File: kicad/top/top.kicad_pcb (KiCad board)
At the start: 2 copper layers, 65 x 120 mm, 34 parts, among them J1 OLED_128x32, J2 Conn_01x15, SW1 SLW-864574-5A-RA-N-D, SW2 RotaryEncoder_Switch

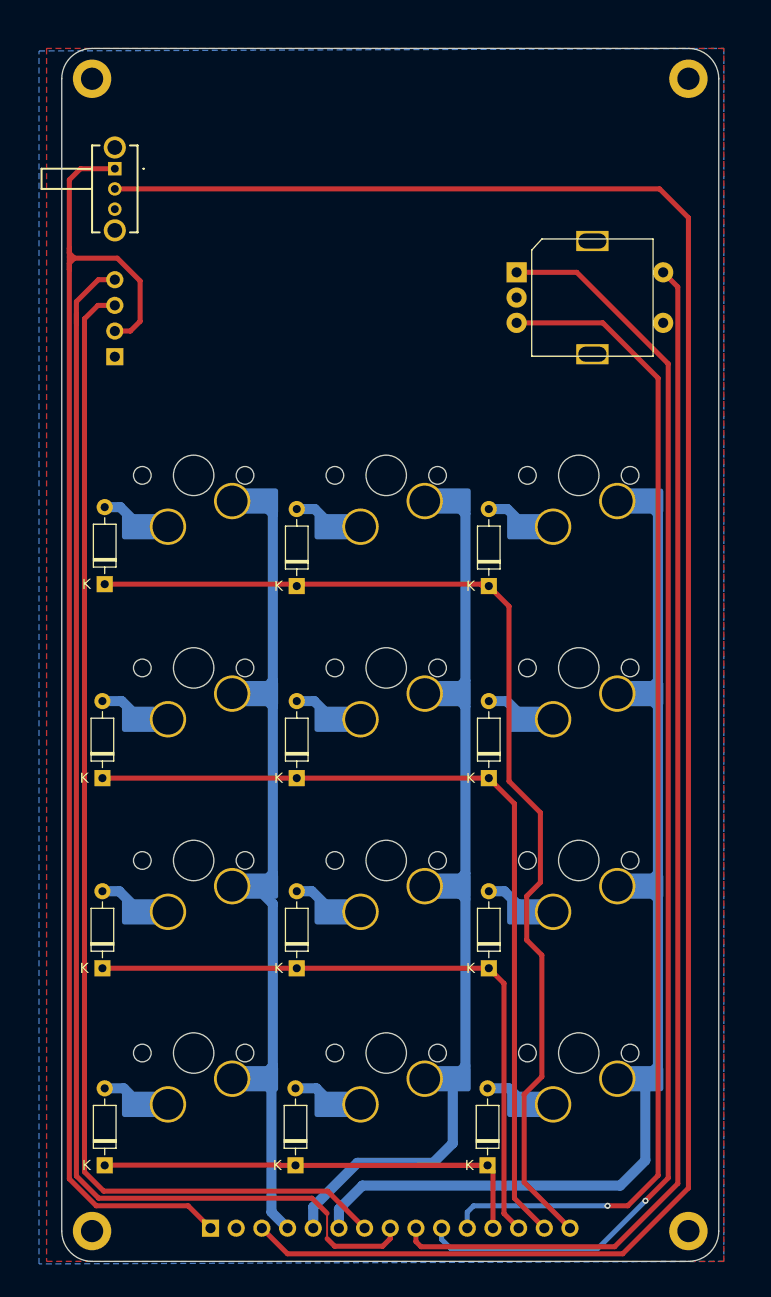
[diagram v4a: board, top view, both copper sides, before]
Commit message: Update KiCad project files and documentation
- Adjusted pad dimensions in top.kicad_pro:
  - Drill size changed from 1.0 to 0.8
  - Height changed from 1.7 to 1.6
  - Width changed from 1.7 to 2.0
- Modified design rule for isolated copper from "warning" to "ignore"
- Increased minimum hole clearance from 0.16 to 0.25

- Corrected global label positions for OLED_SDA and OLED_SCL in top.kicad_sch
- Updated footprint properties for mounting holes in top.kicad_sch to "MountingHole:MountingHole_2.5mm_Pad"

- Created new documentation file for component details.
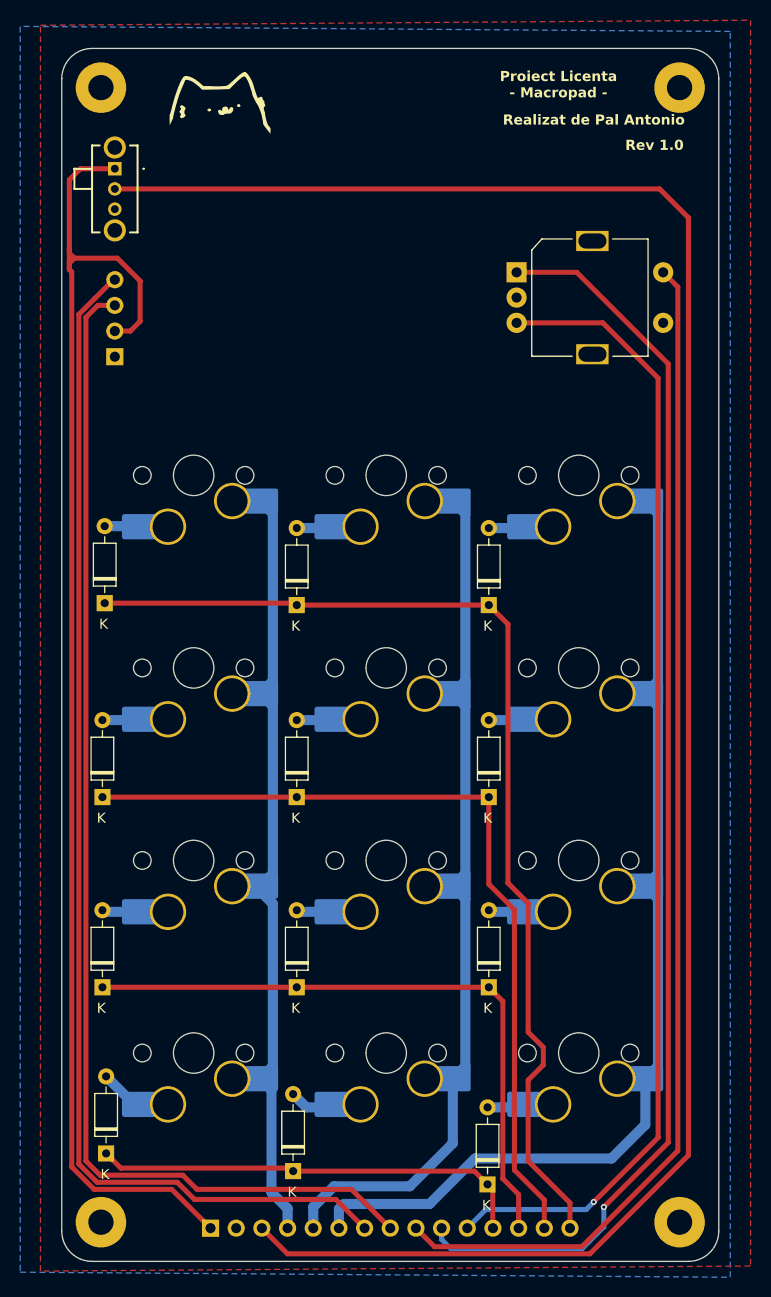
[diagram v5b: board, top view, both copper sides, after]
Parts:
- removed G***: LOGO, Project-Footprints:nubcat_10mm
- removed G***: LOGO, Project-Footprints:nubcat4_24mm
- added REF**: LOGO, Top-Footprints:nubcat_10mm, F.Cu at (133.3, 31.6)
- H1, H2, H3, H4: footprint Top-Footprints:MountingHole_2.2mm_M2_DIN965_Pad -> MountingHole:MountingHole_2.5mm_Pad
- moved D1 1.88 mm to (121.9, 80.9)
- moved D2 1.88 mm to (140.9, 81.1)
- moved D3 1.88 mm to (159.9, 81.1)
- moved D4 1.88 mm to (121.7, 100.1)
- moved D5 1.88 mm to (140.9, 100.1)
- moved D6 1.88 mm to (159.9, 100.1)
- moved D7 1.88 mm to (121.7, 118.9)
- moved D8 1.88 mm to (140.9, 118.9)
- moved D9 1.88 mm to (159.9, 118.9)
- moved D12 1.88 mm to (159.8, 138.4)
- moved H3 1.24 mm to (121.5, 142.2)
- moved H4 1.24 mm to (178.8, 142.2)
- moved H1 1.24 mm to (178.8, 29.9)
- moved H2 1.24 mm to (121.5, 29.9)
- moved D10 1.19 mm to (122.0, 135.4)
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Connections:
- J2 pad 7: OLED_SCL -> OLED_SDA
- J2 pad 8: OLED_SDA -> OLED_SCL
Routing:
- net OLED_SDA: track 128.9 -> 119.9 mm
- net ROW3: track 51.2 -> 42.8 mm
- net ROW0: track 107.5 -> 103.9 mm
- net ENC_DT: track 117.1 -> 114.0 mm
- net ENC_SW: track 120.8 -> 118.1 mm
- net COL2: track 102.5 -> 100.5 mm
- net BT_SELECT: track 199.9 -> 198.0 mm
- net ROW2: track 65.2 -> 63.3 mm
- net ROW1: track 85.0 -> 83.1 mm
- net OLED_SCL: track 118.0 -> 119.7 mm
- net Net-(D8-A): track 4.37 -> 3.37 mm
- net Net-(D7-A): track 4.55 -> 3.55 mm
- net Net-(D9-A): track 4.42 -> 3.42 mm
- net Net-(D12-A): track 4.36 -> 3.41 mm
- net ENC_CLK: track 126.1 -> 125.2 mm
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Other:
- board text added: "Proiect Licenta - Macropad -"
- board text added: "Realizat de Pal Antonio"
- board text added: "Rev 1.0"
